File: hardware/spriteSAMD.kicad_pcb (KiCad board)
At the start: 2 copper layers, 47.2 x 35 mm, 87 parts, among them J1 10118194-0001LF, J10 Conn_01x04, J11 Conn_01x01, J12 Conn_01x01, J13 Conn_01x01, J14 Conn_01x01, J15 Conn_01x01, J16 Conn_01x01, J17 Conn_01x02, J18 Conn_01x02, J19 Conn_01x01, J2 Conn_01x04, J20 Conn_01x01, J21 Conn_01x02, J24 Conn_01x01, J25 Conn_01x02, J26 Conn_01x02, J27 Conn_01x02, J28 Conn_01x01, J29 Conn_01x02, J3 Conn_01x04, J4 Conn_01x04, J5 Conn_01x04, J6 Conn_01x04, J7 Conn_01x04, J8 Conn_01x04, J9 Conn_01x04, SW2 KMR231NG LFS, U1 BAT-HLD-001, U2 CC1101RGPR, U3 LSM9DS1, U4 TPS82740ASIP, U6 ATSAMD51G_TQFN48, U7 OVM9724, U8 DS90LV012ATMFX_NOPB, U9 DS90LV012ATMFX_NOPB, X1 ST3215SB

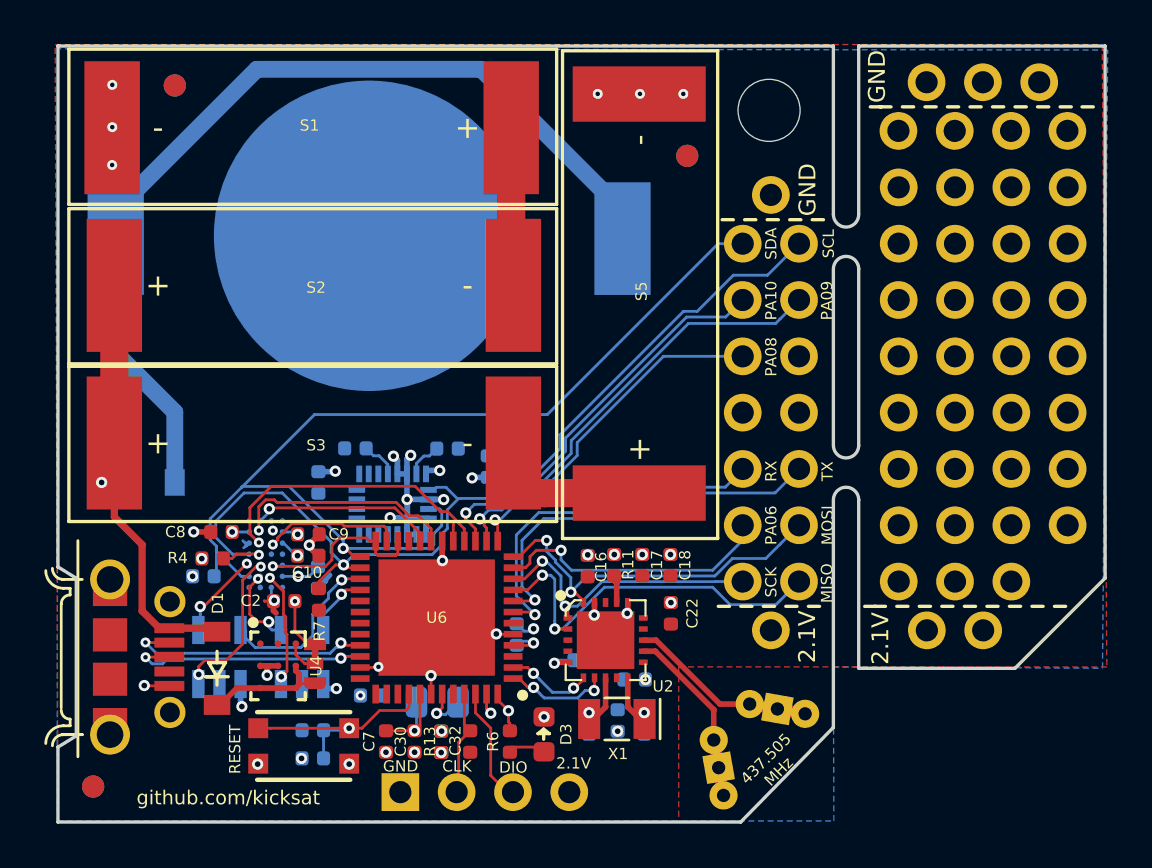
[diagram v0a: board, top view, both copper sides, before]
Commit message: updating to v2b (TXCO added)
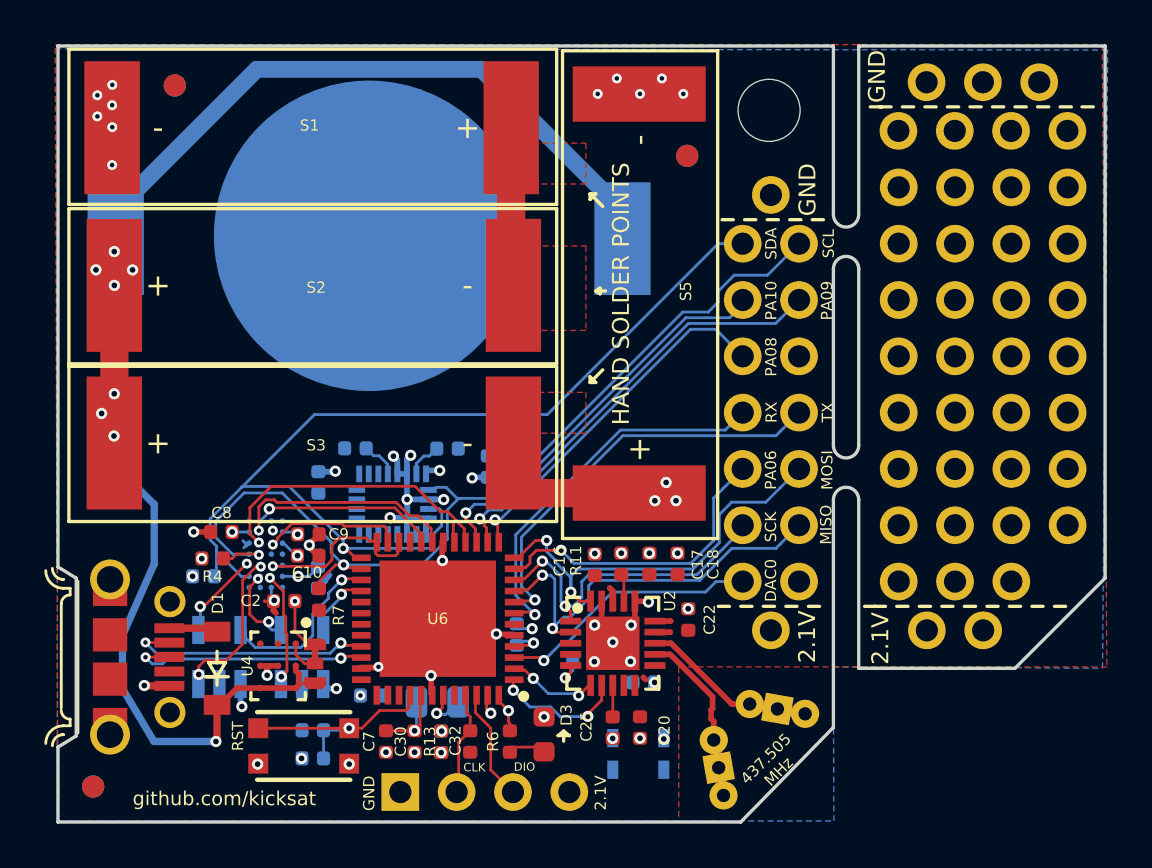
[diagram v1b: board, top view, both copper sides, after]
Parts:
- removed C26: 27pF, Capacitor_SMD:C_0402_1005Metric
- removed D2: MBR120, Diode_SMD:D_SOD-123
- removed J28: Conn_01x01, custom-footprints:PinHeader_CUSTOM2
- removed J29: Conn_01x02, custom-footprints:PinHeader_CUSTOM3
- added J22: Conn_01x02, custom-footprints:PinHeader_CUSTOM3, F.Cu at (112.6, 88.0)
- added J23: Conn_01x02, custom-footprints:PinHeader_CUSTOM3, F.Cu at (112.6, 85.5)
- C20, C25: moved to F.Cu
- C7: value 10uF -> 1uF
- J10, J2, J4, J5, J6, J7, J8, J9: value Conn_01x04 -> Conn_01x01; footprint custom-footprints:PinHeader_CUSTOM -> custom-footprints:PinHeader_CUSTOM2
- J13, J14, J15, J16, J19, J20: value Conn_01x01 -> Conn_01x04; footprint custom-footprints:PinHeader_CUSTOM2 -> custom-footprints:PinHeader_CUSTOM
- J17, J18: value Conn_01x02 -> Conn_01x04; footprint custom-footprints:PinHeader_CUSTOM3 -> custom-footprints:PinHeader_CUSTOM
- J24: value Conn_01x01 -> Conn_01x02; footprint custom-footprints:PinHeader_CUSTOM2 -> custom-footprints:PinHeader_CUSTOM3
- R6: value 2.2K -> 330
- U2: footprint digikey-footprints:QFN-20-1EP_4x4mm_RevA -> custom-footprints:CC1101_RGP_20
- X1: value ST3215SB -> 26.000; footprint Crystal:Crystal_SMD_MicroCrystal_CC7V-T1A-2Pin_3.2x1.5mm -> custom-footprints:TXCO_2.5x2; moved to B.Cu
- moved J12 25.2 mm to (126.0, 75.7)
- moved J11 24.9 mm to (123.5, 100.4)
- moved J4 20.5 mm to (122.2, 98.2), turned to 0 degrees
- moved J13 17.9 mm to (119.6, 93.1), turned to 90 degrees
- moved J2 17.8 mm to (119.6, 98.2), turned to 0 degrees
- moved J20 17.8 mm to (119.6, 80.4), turned to 90 degrees
- moved J5 16.1 mm to (124.7, 98.2), turned to 0 degrees
- moved J10 16.0 mm to (113.9, 80.8), turned to 0 degrees
- moved J6 16.0 mm to (113.9, 100.4), turned to 0 degrees
- moved J27 15.2 mm to (112.6, 98.2)
- moved J8 15.0 mm to (120.9, 75.7), turned to 0 degrees
- moved J18 14.5 mm to (119.6, 83.0)
- moved J16 13.9 mm to (119.6, 88.0), turned to 90 degrees
- moved J7 12.9 mm to (123.4, 75.7), turned to 0 degrees
- moved J14 11.4 mm to (119.6, 90.6), turned to 90 degrees
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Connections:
- net CC1101_CS renamed radioCS
- C25 pad 2: GND -> Net-(C25-Pad2)
- C8 pad 1: +2V1 -> /AVDD
- J10 pad 1: Net-(J10-Pad1) -> GND
- J11 pad 1: GND -> +2V1
- J12 pad 1: +2V1 -> GND
- J13 pad 1: GND -> Net-(J13-Pad1)
- J14 pad 1: +2V1 -> Net-(J14-Pad1)
- J15 pad 1: +2V1 -> Net-(J15-Pad1)
- J16 pad 1: GND -> Net-(J16-Pad1)
- J17 pad 1: RX -> Net-(J17-Pad1)
- J17 pad 2: TX -> Net-(J17-Pad2)
- J18 pad 1: PA06 -> Net-(J18-Pad1)
- J18 pad 2: MOSI -> Net-(J18-Pad2)
- J19 pad 1: GND -> Net-(J19-Pad1)
- J21 pad 1: PA08 -> SCK
- J21 pad 2: Net-(J21-Pad2) -> MISO
- J24 pad 1: Net-(J24-Pad1) -> PA06
- J25 pad 1: Net-(J25-Pad1) -> RX
- J25 pad 2: Net-(J25-Pad2) -> TX
- J26 pad 1: PA10 -> SDA
- J26 pad 2: PA09 -> SCL
- J27 pad 1: SDA -> DAC0
- J27 pad 2: SCL -> Net-(J27-Pad2)
- J6 pad 1: Net-(J6-Pad1) -> +2V1
- J7 pad 1: Net-(J7-Pad1) -> GND
- J8 pad 1: Net-(J8-Pad1) -> GND
- J9 pad 1: Net-(J9-Pad1) -> +2V1
- S2 pad 1: VUSB -> Net-(D1-Pad1)
- S3 pad 1: VUSB -> Net-(D1-Pad1)
- U1 pad 1: Net-(D2-Pad2) -> Net-(D1-Pad1)
- U1 pad 3: Net-(D2-Pad2) -> Net-(D1-Pad1)
- U2 pad 10: Net-(C26-Pad1) -> Net-(U2-Pad10)
- U6 pad 3: Net-(U6-Pad3) -> DAC0
- U7 pad A2: +2V1 -> /AVDD
- X1 pad 1: Net-(C26-Pad1) -> GND
- X1 pad 2: Net-(C25-Pad1) -> GND
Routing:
- net Net-(D1-Pad1): track 5.94 -> 64.9 mm, vias 0 -> 8
- net Net-(D2-Pad2): track 42.8 -> 0.00 mm
- net VUSB: track 19.0 -> 2.22 mm, vias 1 -> 0
- net DAC0: track 0.00 -> 12.5 mm, vias 0 -> 1
- net MOSI: track 16.9 -> 19.4 mm
- net Net-(C26-Pad1): track 2.37 -> 0.00 mm, vias 1 -> 0
- net SCK: track 13.3 -> 15.0 mm
- net Net-(S3-Pad2): track 5.43 -> 7.11 mm, vias 0 -> 3
- net Net-(S1-Pad1): track 7.37 -> 5.80 mm
- net GND: track 13.4 -> 14.9 mm, vias 29 -> 39
- net radioCS: track 4.73 -> 6.05 mm
- net PA06: track 12.7 -> 14.0 mm
- net TX: track 17.8 -> 18.9 mm
- net MISO: track 17.6 -> 18.8 mm
- net +2V1: track 20.6 -> 21.7 mm, vias 21 -> 20
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- added copper zone on B.Cu, net Net-(D1-Pad1)
- added copper zone on F.Cu, net Net-(S1-Pad1)
- added copper zone on B.Cu, net Net-(S3-Pad2)
- added copper zone on F.Cu, net Net-(S3-Pad2)
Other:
- rule pad_to_mask_clearance: 0.2 -> 0.0508
- rule solder_mask_min_width: 0.1016 -> 0.0508
- board text added: "C+M"
- board text added: "CR2032 -- UNPLUG USB"
- board text added: "DAC0"
- board text added: "HAND SOLDER POINTS"
- board text added: "RST"
- board text added: "v2b"
- board text removed: "RESET"

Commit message: Via drills changed 0.25 to 0.3 mm
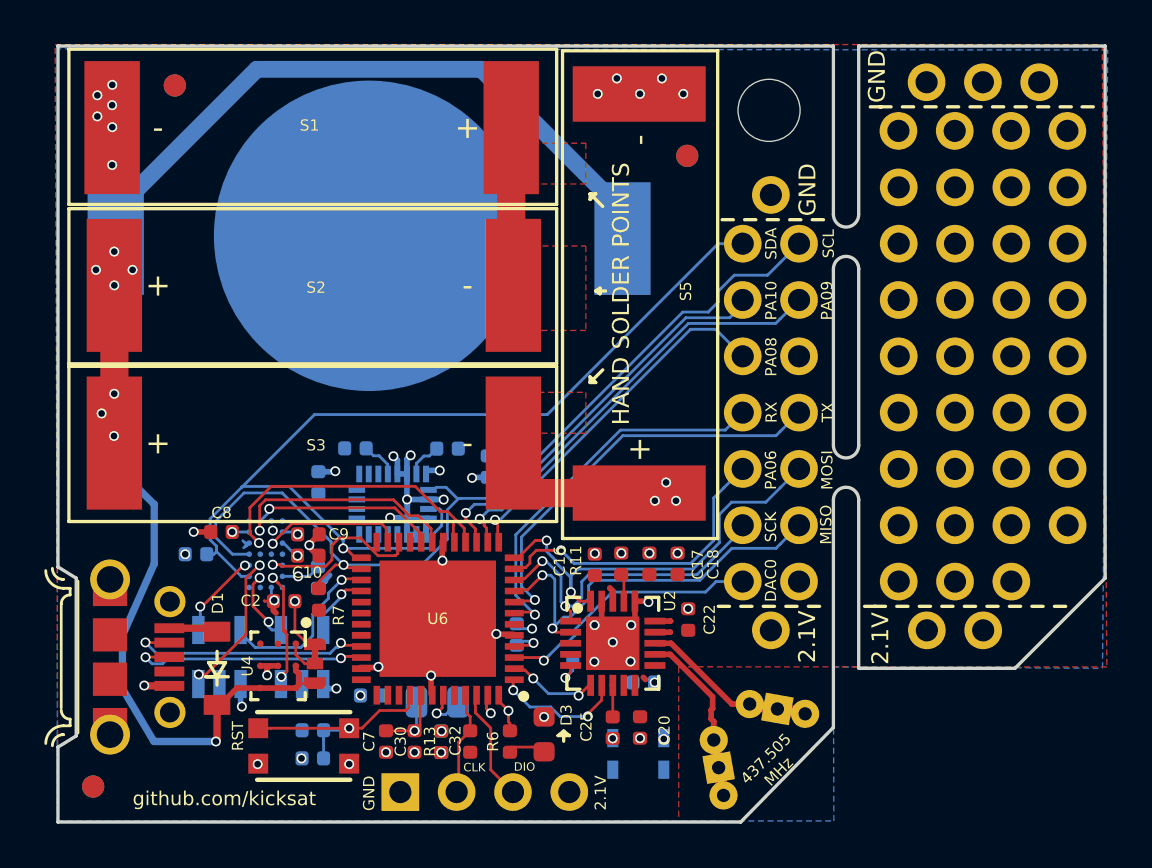
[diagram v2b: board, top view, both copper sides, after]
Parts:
- removed R4: 10K, Resistor_SMD:R_0402_1005Metric
- moved R8 1.05 mm to (88.0, 97.0)
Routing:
- net Net-(U7-PadB4): track 1.91 -> 0.00 mm, vias 1 -> 0
- net SDA: track 47.2 -> 46.5 mm
- net GND: vias 39 -> 38
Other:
- net class Default: via_dia 0.508 -> 0.45; via_drill 0.254 -> 0.3
- net class PCC: via_drill 0.2 -> 0.3
- net class PWR: via_dia 0.508 -> 0.45; via_drill 0.254 -> 0.3
- rule via_min_drill: 0.2 -> 0.3

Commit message: silly fixes for fab house
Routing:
- net SHDWN: track 10.3 -> 0.00 mm, vias 1 -> 0
- net MD: track 7.69 -> 11.5 mm
- net GND: track 14.9 -> 14.3 mm
- net FSYNC: track 7.59 -> 8.17 mm
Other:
- net class Default: trace_width 0.127 -> 0.0889
- net class PCC: clearance 0.0889 -> 0.127
- net class PWR: clearance 0.0889 -> 0.127; trace_width 0.254 -> 0.0889
- rule via_min_drill: 0.3 -> 0.25
